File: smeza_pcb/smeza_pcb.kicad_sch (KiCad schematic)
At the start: 55 parts, among them J1 SS-90000-002, J2 SS-90000-002, J3 Conn_01x03, J4 Conn_01x04, J5 Conn_01x03, J6 Conn_01x03, J7 Conn_01x03, J8 Conn_01x03, J9 Conn_02x03_Odd_Even, SW1 SW_DIP_x04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

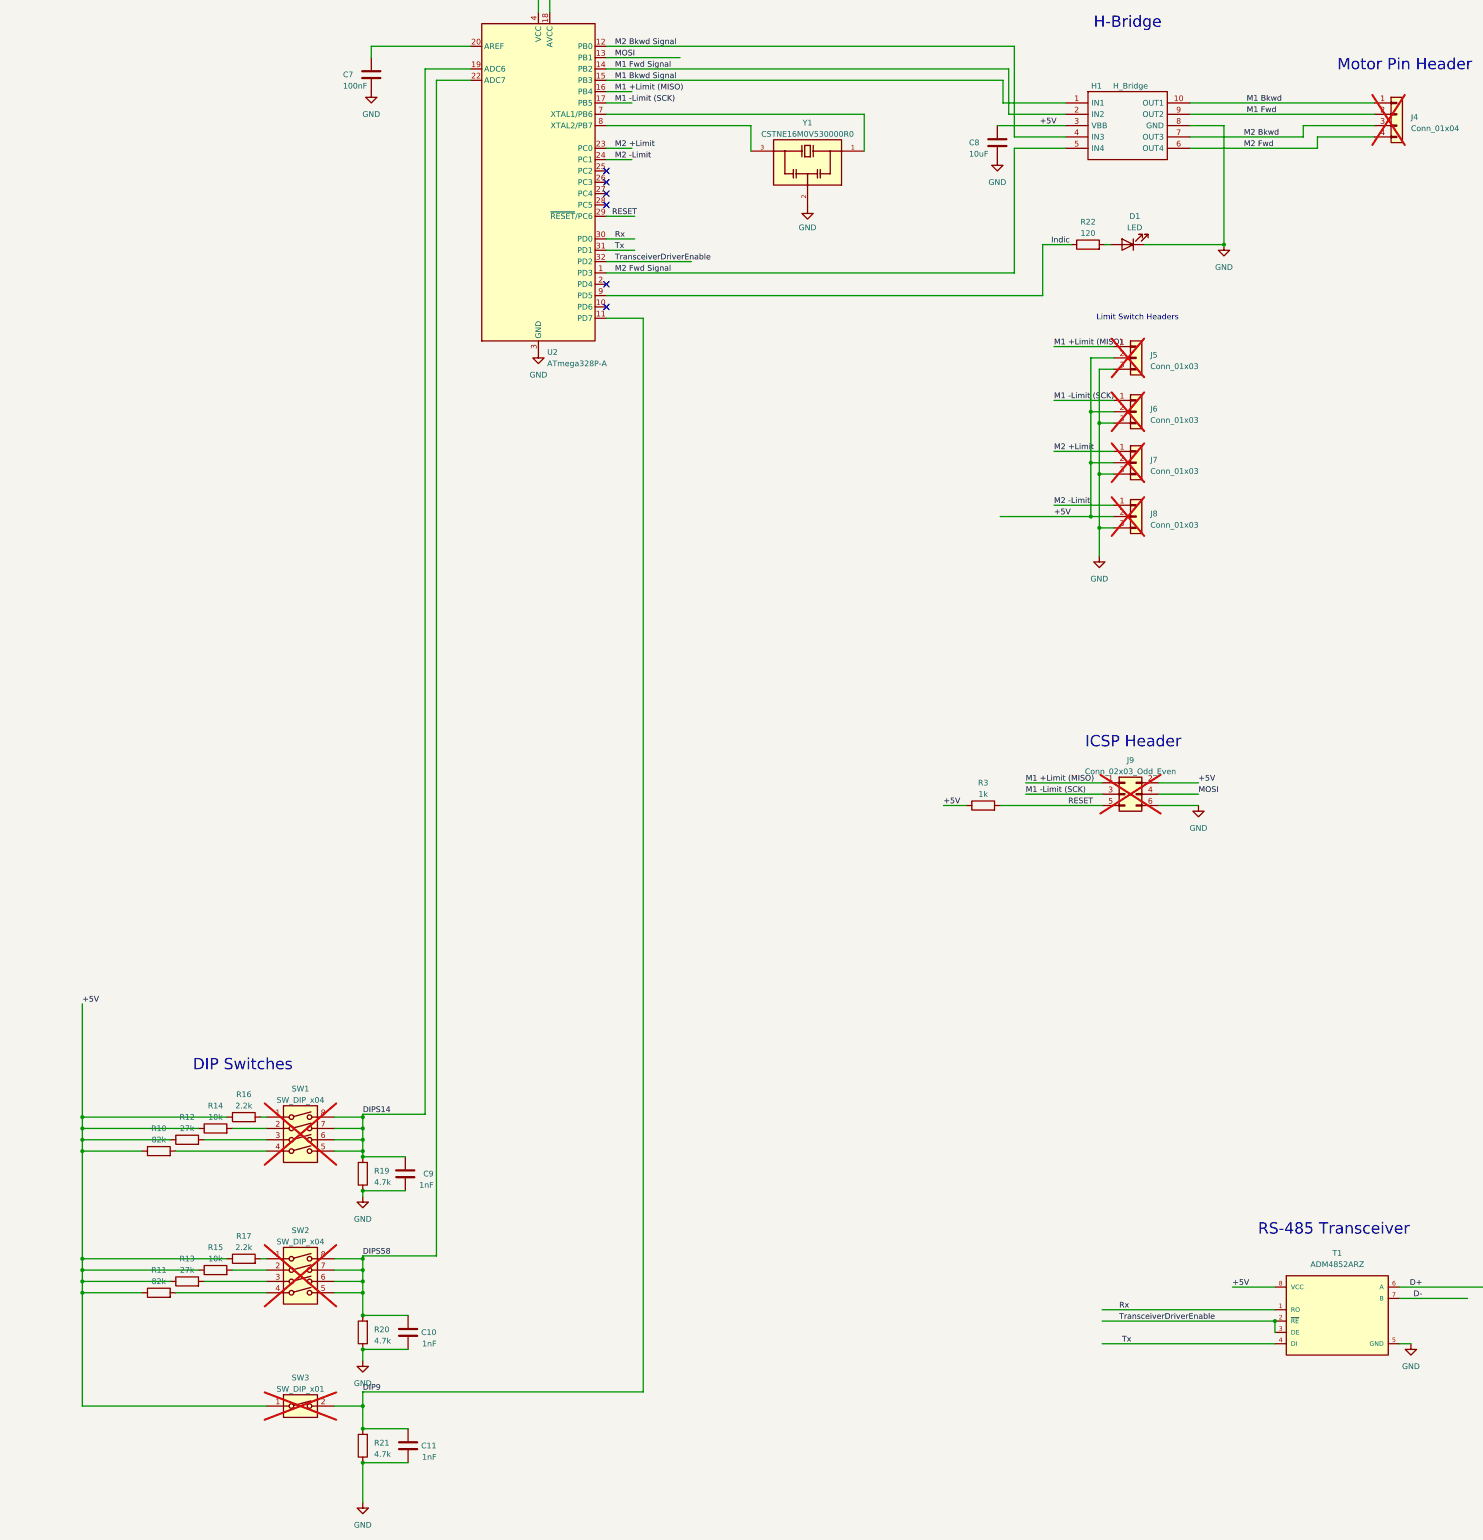
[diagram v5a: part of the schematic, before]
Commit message: Fixed part rotations. Fixed silkscreen goofs. Added solder jumpers.
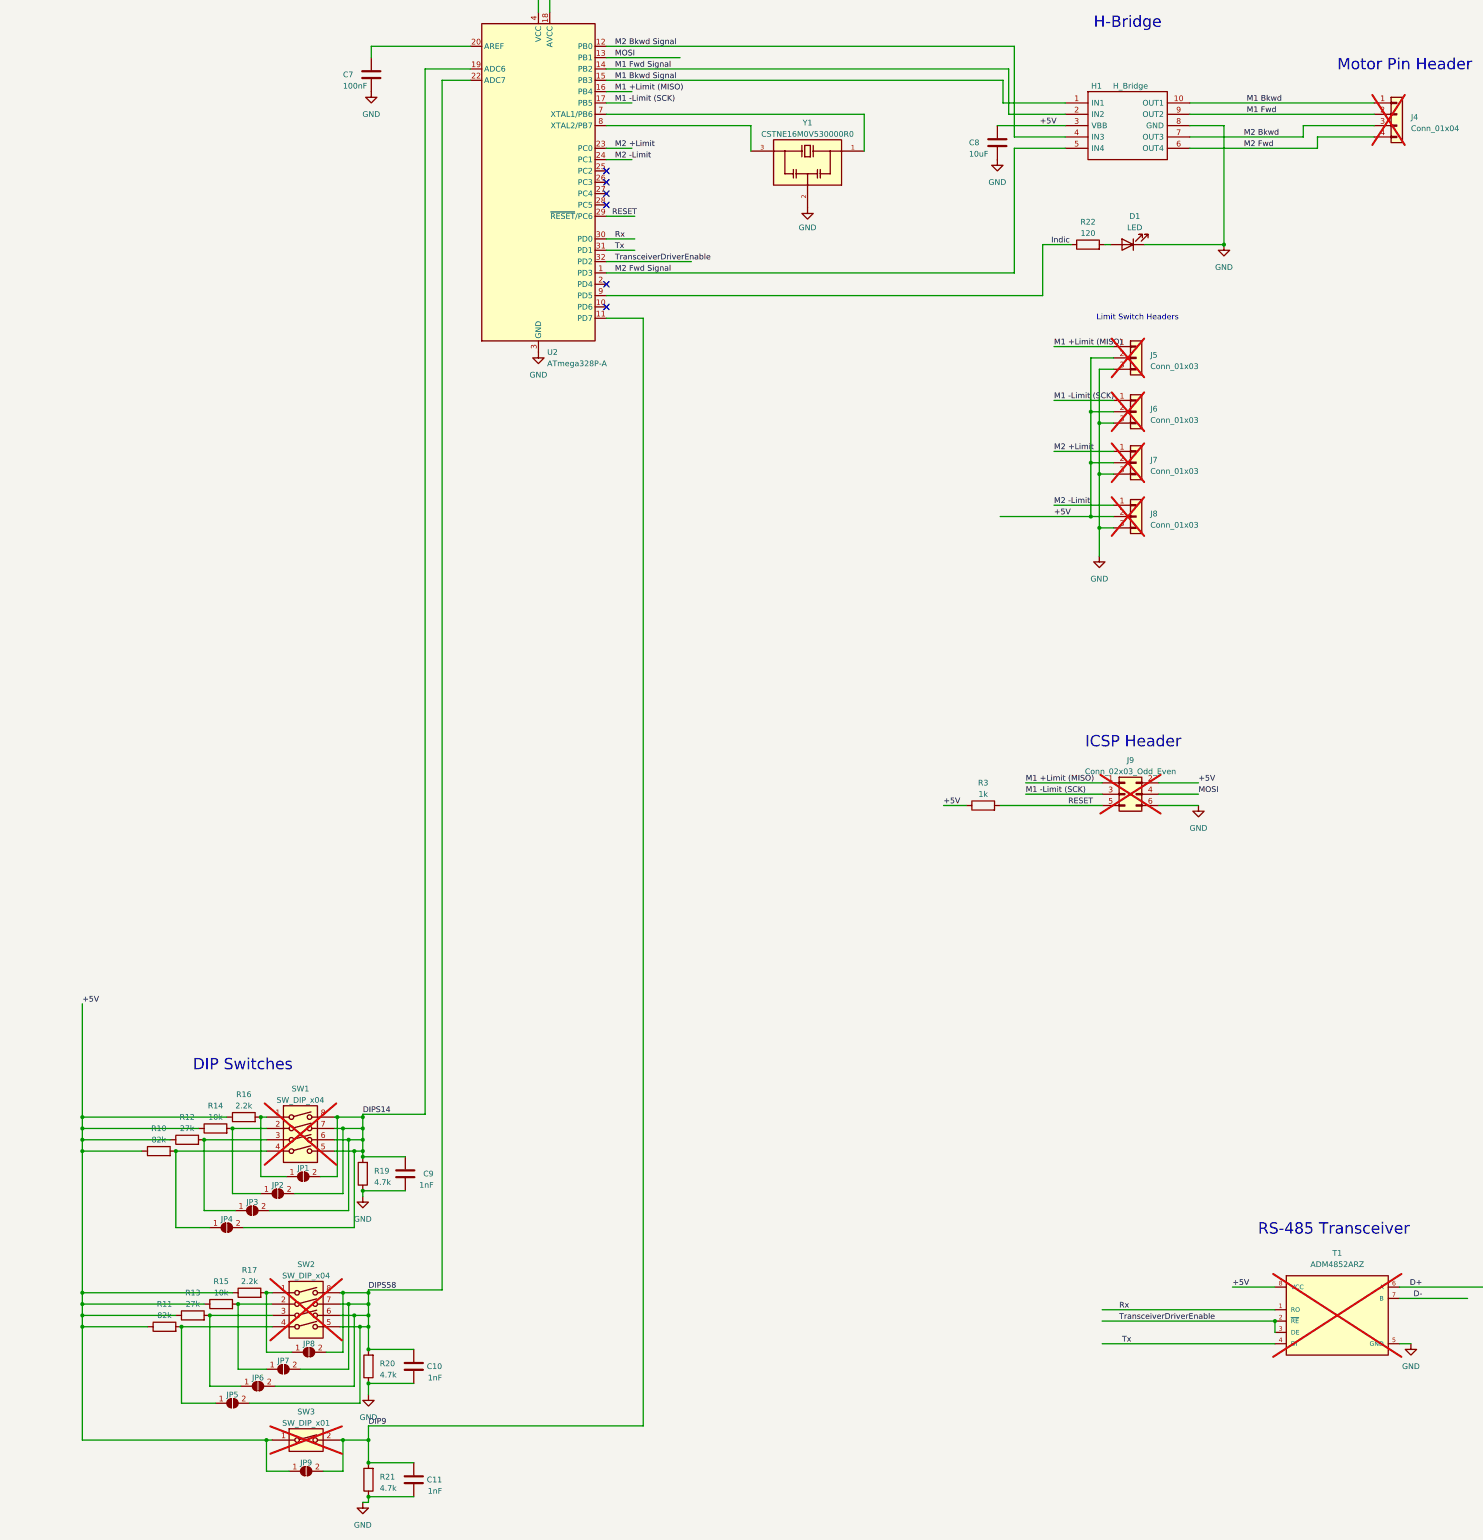
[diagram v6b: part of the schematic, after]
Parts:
- added JP1, JP2, JP3, JP4, JP5, JP6, JP7, JP8, JP9: SolderJumper_2_Open, Jumper:SolderJumper-2_P1.3mm_Open_TrianglePad1.0x1.5mm, symbol Jumper:SolderJumper_2_Open
- J1, J2, J3, J4, J5, J6, J7, J8, J9, SW1, SW2, SW3: now left out of the parts list
- T1: now not fitted; now left out of the parts list
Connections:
- net +5V: now also JP9.1 (A)
- net DIP9: now also JP9.2 (B)
- net DIPS14: now also JP1.2 (B), JP2.2 (B), JP3.2 (B), JP4.2 (B)
- net DIPS58: now also JP5.2 (B), JP6.2 (B), JP7.2 (B), JP8.2 (B)
- net at R13.2, SW2.3: now also JP6.1 (A)
- net at R16.2, SW1.1: now also JP1.1 (A)
- net at R14.2, SW1.2: now also JP2.1 (A)
- net at R12.2, SW1.3: now also JP3.1 (A)
- net at R10.2, SW1.4: now also JP4.1 (A)
- net at R17.2, SW2.1: now also JP8.1 (A)
- net at R15.2, SW2.2: now also JP7.1 (A)
- net at R11.2, SW2.4: now also JP5.1 (A)
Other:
- moved on the sheet: C10, C11, R11, R13, R15, R17, R20, R21, SW2, SW3
